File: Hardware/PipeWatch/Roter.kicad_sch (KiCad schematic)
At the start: 3 parts

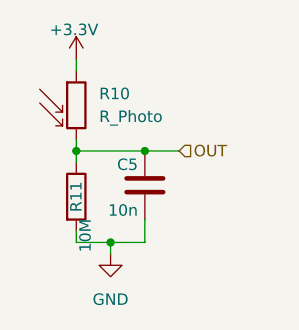
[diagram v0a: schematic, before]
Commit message: Started laying traces
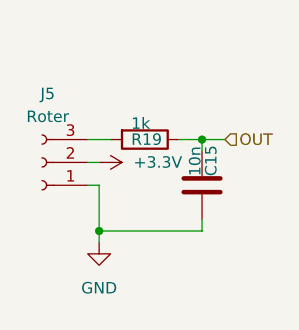
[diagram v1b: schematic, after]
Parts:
- removed C5: 10n, Capacitor_SMD:C_0603_1608Metric, symbol Device:C
- removed R10: R_Photo, OptoDevice:R_LDR_5.0x4.1mm_P3mm_Vertical, symbol Device:R_Photo
- removed R11: 10M, Resistor_SMD:R_0603_1608Metric, symbol Device:R
- added C15: 10n, Capacitor_SMD:C_0603_1608Metric, symbol Device:C
- added J5: Roter, Connector_PinHeader_2.54mm:PinHeader_1x03_P2.54mm_Vertical, symbol Connector:Conn_01x03_Socket
- added R19: 1k, Resistor_SMD:R_0603_1608Metric, symbol Device:R
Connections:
- net +3.3V: now also J5.2 (Pin_2)
- net GND: now also C15.2, J5.1 (Pin_1)
- net OUT: now also C15.1, R19.1
- new net: J5.3 (Pin_3), R19.2

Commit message: Changed the scematic page Labeling
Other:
- company: (none) -> Felix Pelster
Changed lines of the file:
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@@
 	(generator_version "9.0")
 	(paper "A4")
+	(title_block
+		(date "2025-09-24")
+		(company "Felix Pelster")
+	)
 	(junction
 		(at 129.54 100.33)
